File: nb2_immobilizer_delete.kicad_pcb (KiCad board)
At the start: 2 copper layers, 75.5 x 18.5 mm, 7 parts, among them J1 AVR-ISP-6, P1 1123038-2, Q1 BC849, Q2 BC849, U1 ATtiny85-20S

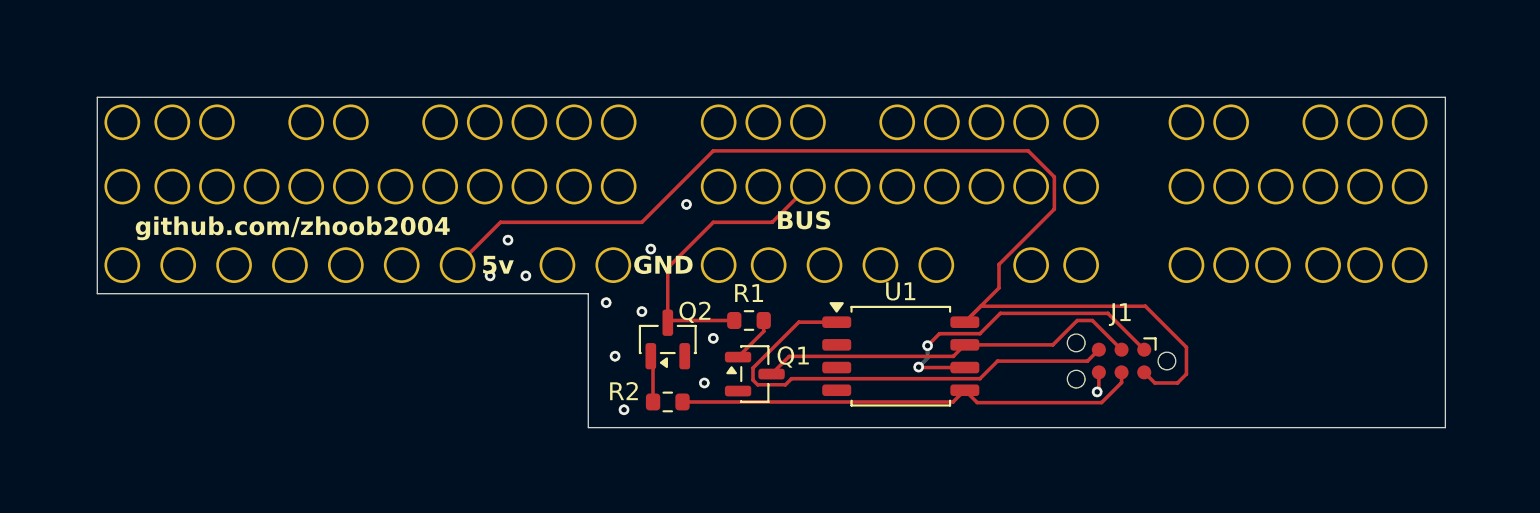
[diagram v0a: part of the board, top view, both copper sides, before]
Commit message: added capacitor, dnp tag-connect
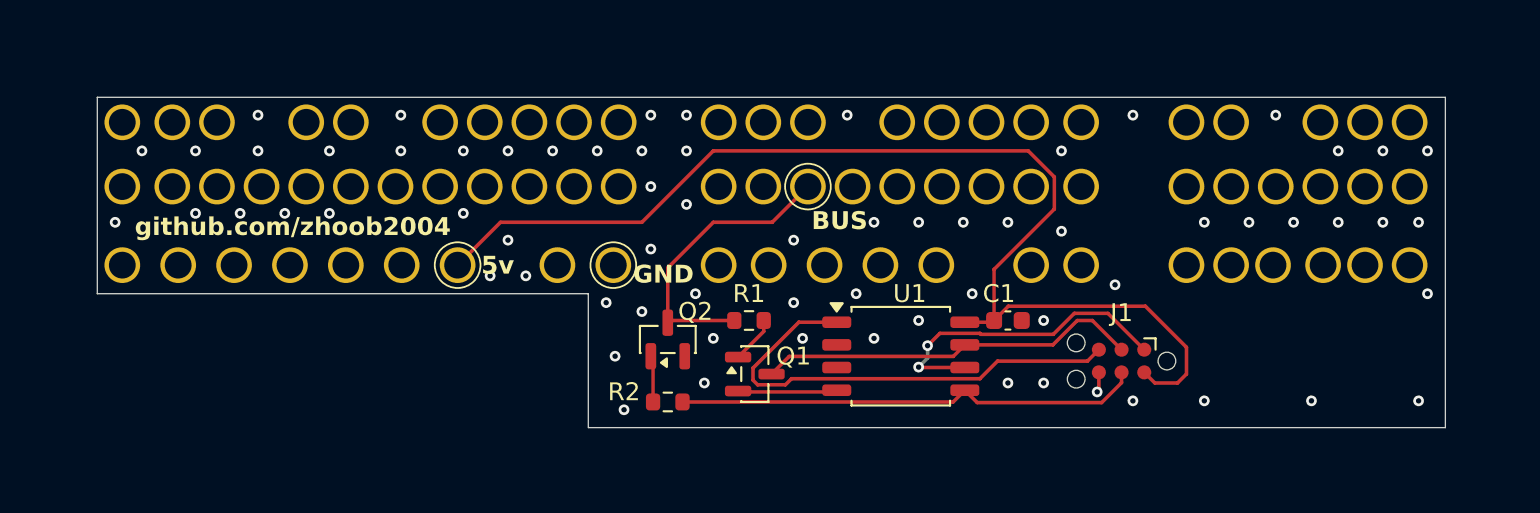
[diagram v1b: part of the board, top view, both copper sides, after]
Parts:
- added C1: 100nf, Capacitor_SMD:C_0603_1608Metric, F.Cu at (153.0, 92.0)
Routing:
- net GND: track 1.13 -> 6.72 mm, vias 12 -> 69
- net +5V: track 64.9 -> 64.2 mm

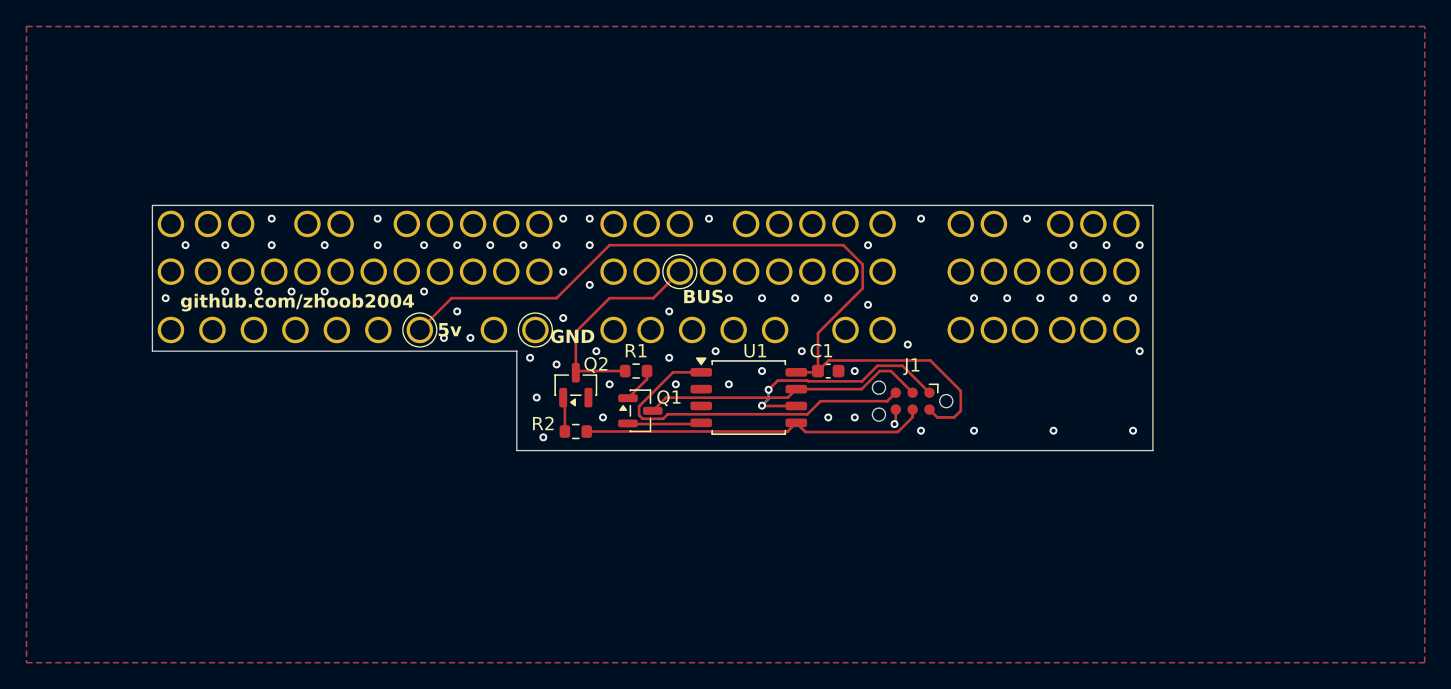
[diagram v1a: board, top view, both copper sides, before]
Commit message: revised layout for robustness, reduced clock to 1mhz, added github actions workflow
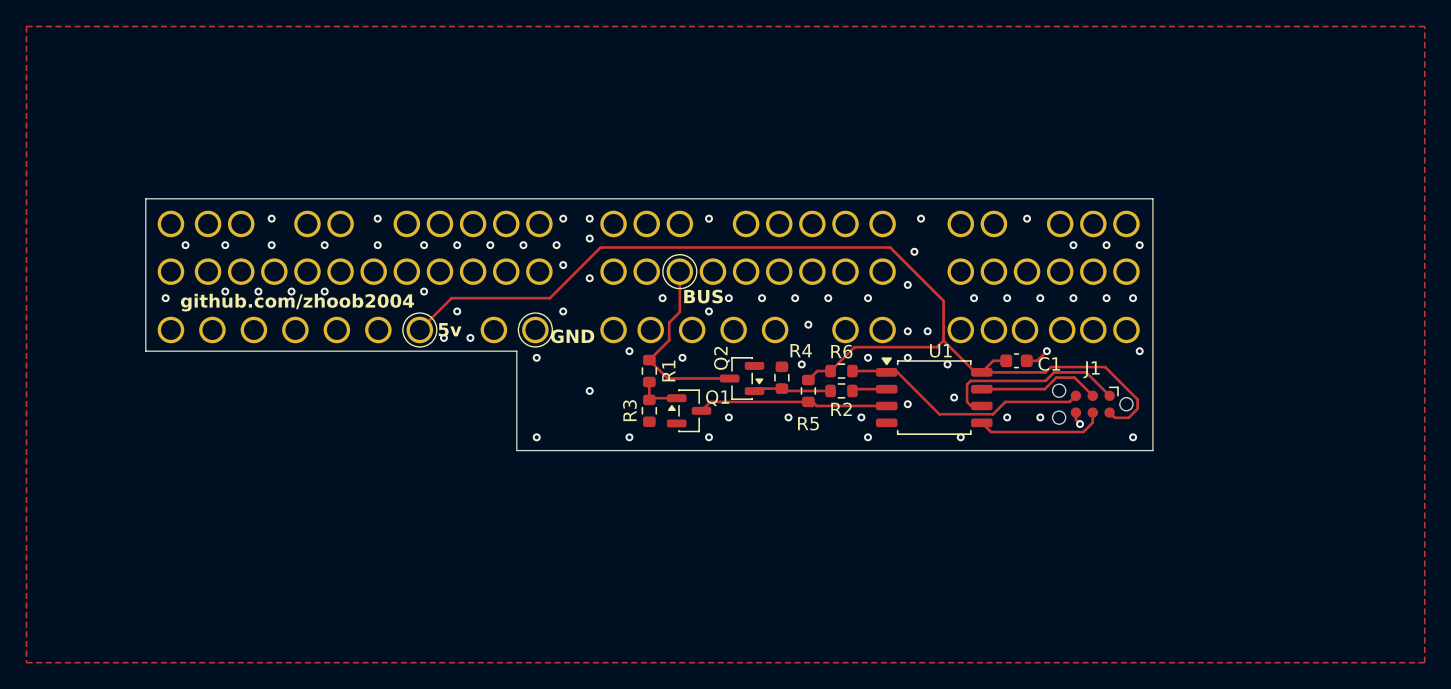
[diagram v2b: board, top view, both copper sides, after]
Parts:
- added R3: 100k, Resistor_SMD:R_0603_1608Metric, F.Cu at (139.5, 95.0)
- added R4: 100k, Resistor_SMD:R_0603_1608Metric, F.Cu at (149.5, 92.5)
- added R5: 10k, Resistor_SMD:R_0603_1608Metric, F.Cu at (151.5, 93.5)
- added R6: 10k, Resistor_SMD:R_0603_1608Metric, F.Cu at (154.0, 92.0)
- R1: value 150k -> 100k
- R2: value 1.5k -> 10k
- moved R2 20.3 mm to (154.0, 93.5), turned to 180 degrees
- moved C1 14.2 mm to (167.2, 91.2)
- moved U1 14.0 mm to (161.0, 94.0)
- moved J1 13.6 mm to (173.0, 94.5)
- moved Q2 12.6 mm to (146.5, 92.6), turned to 180 degrees
- moved Q1 3.68 mm to (142.5, 95.0)
- moved R1 1.00 mm to (139.5, 92.0), turned to 90 degrees
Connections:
- J1 pad 3: /rx_inv -> /PB2
- J1 pad 4: /tx_inv -> /PB0
- R2 pad 1: Net-(Q2-B) -> /tx_inv
- R2 pad 2: /tx_inv -> Net-(Q2-B)
- U1 pad 2: unconnected-(U1-XTAL1/PB3-Pad2) -> /tx_inv
- U1 pad 3: unconnected-(U1-XTAL2/PB4-Pad3) -> /rx_inv
- U1 pad 5: /tx_inv -> /PB0
- U1 pad 7: /rx_inv -> /PB2
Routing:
- net /tx_inv: track 26.2 -> 2.64 mm
- net +5V: track 64.2 -> 80.5 mm
- net /PB0: track 0.00 -> 9.71 mm
- net /PB2: track 0.00 -> 9.30 mm
- net /reset: track 26.7 -> 18.8 mm
- net /rx_inv: track 21.5 -> 14.4 mm
- net GND: track 6.72 -> 2.82 mm, vias 69 -> 75
- net /PB1: track 17.8 -> 14.4 mm, vias 2 -> 0
- net Net-(Q2-B): track 2.61 -> 5.89 mm
- net /bus: track 16.6 -> 14.3 mm
- net Net-(Q1-B): track 2.65 -> 3.46 mm
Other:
- board size 75.5 x 18.5 mm -> 76 x 19 mm
